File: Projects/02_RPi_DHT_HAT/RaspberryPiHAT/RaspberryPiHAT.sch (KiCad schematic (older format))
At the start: 9 parts, among them J1 Raspberry_Pi_2_3, SW1 SW_DPST, U1 DHT22

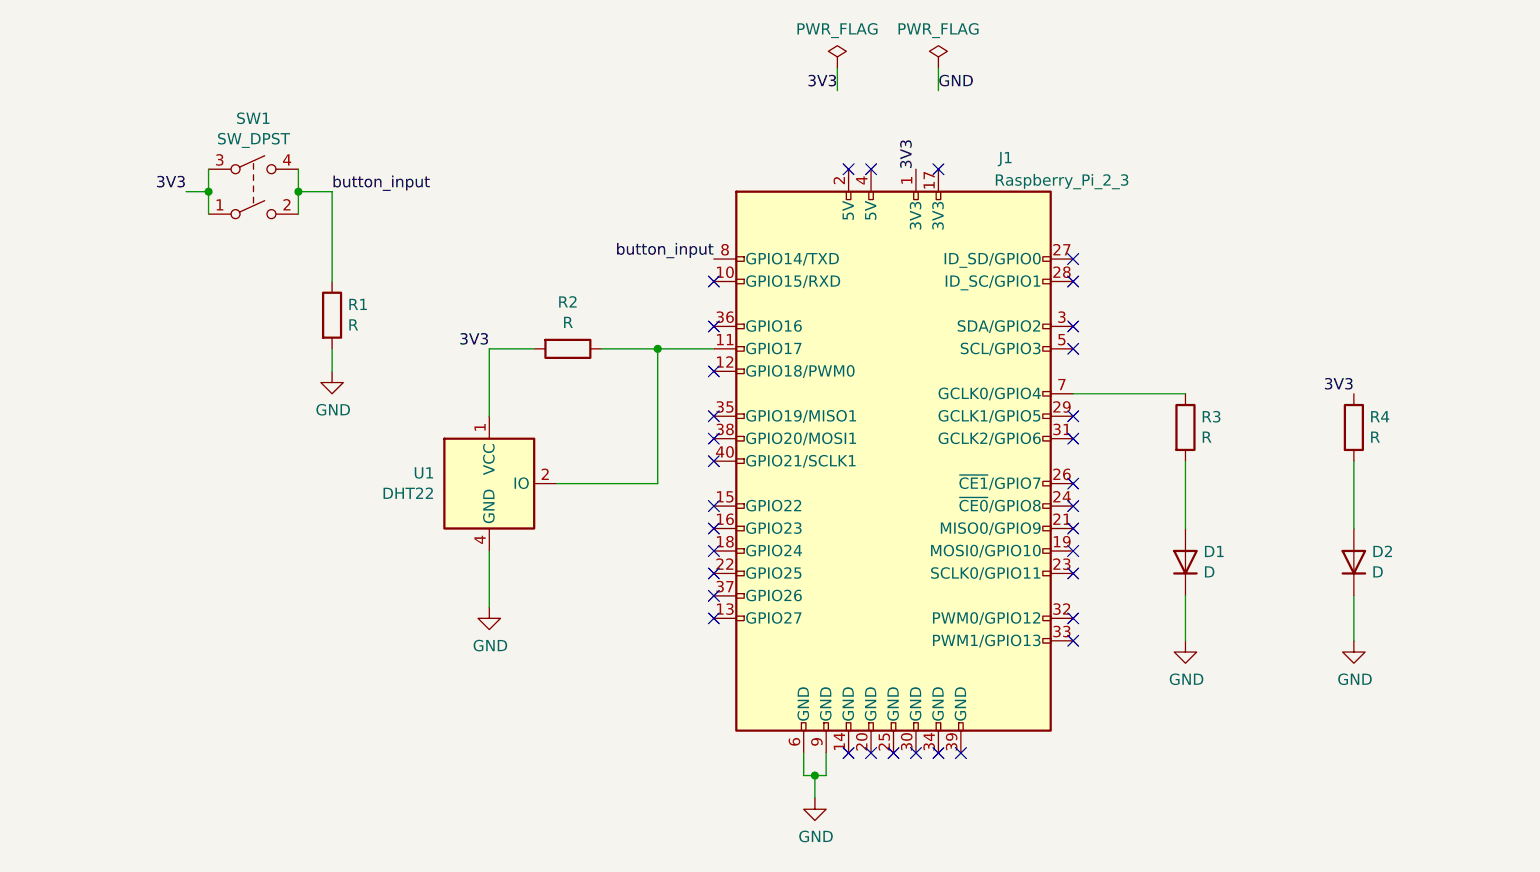
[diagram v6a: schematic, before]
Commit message: Project 2: Add comments on schematic
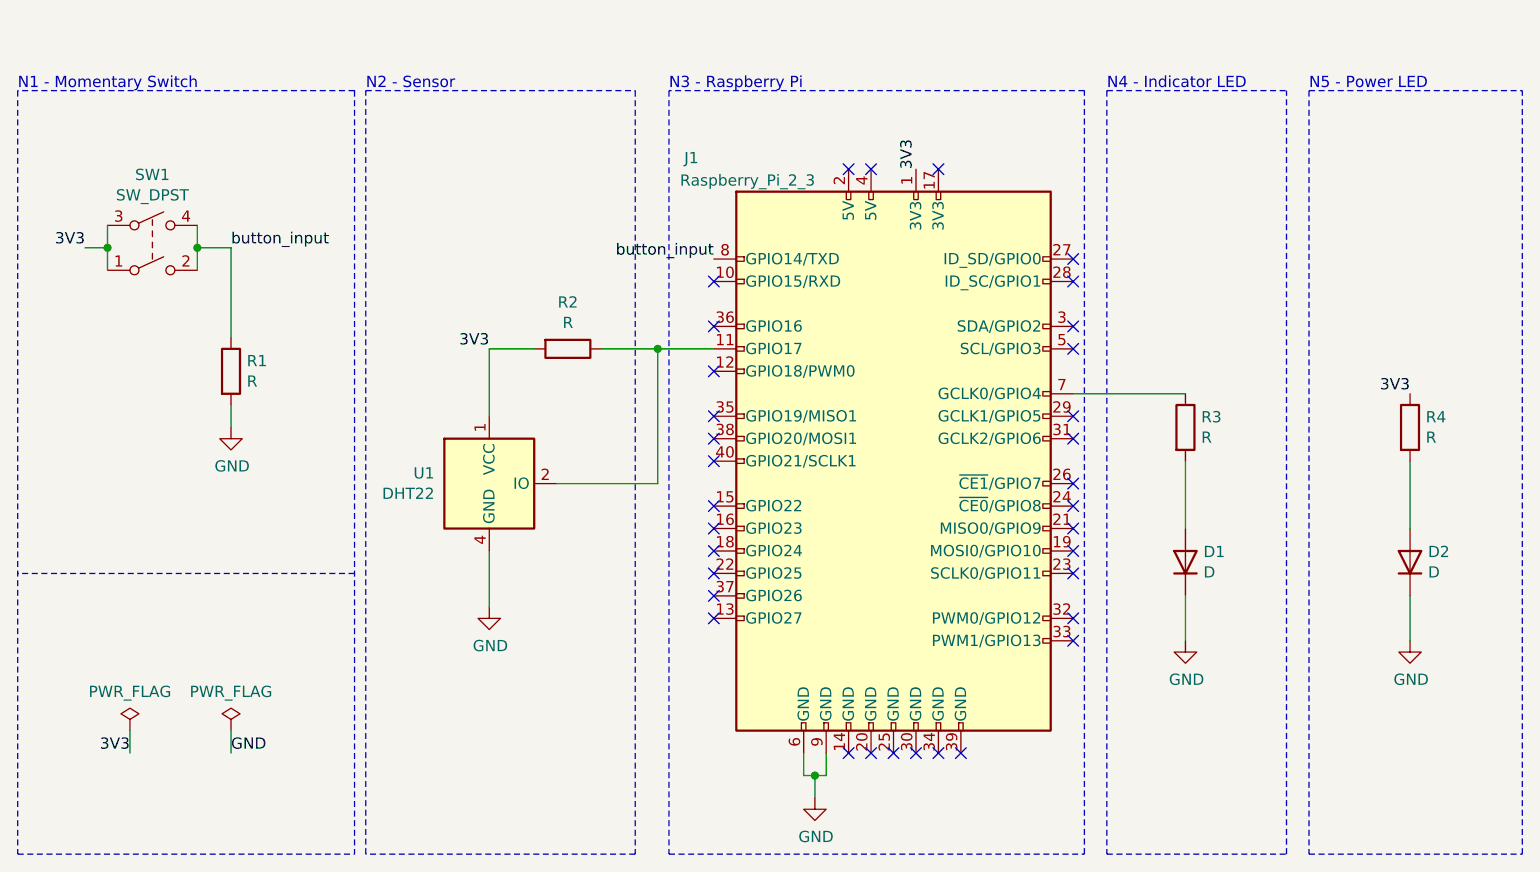
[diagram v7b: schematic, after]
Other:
- note added: "N1 - Momentary Switch"
- note added: "N2 - Sensor"
- note added: "N3 - Raspberry Pi"
- note added: "N4 - Indicator LED"
- note added: "N5 - Power LED"
- moved on the sheet: D2, R1, R4, SW1
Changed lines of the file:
@@
 U 1 1 61CF6995
 P 5550 3750
-F 0 "J1" H 6050 5100 50  0000 C CNN
-F 1 "Raspberry_Pi_2_3" H 6300 5000 50  0000 C CNN
+F 0 "J1" H 4650 5100 50  0000 C CNN
+F 1 "Raspberry_Pi_2_3" H 4900 5000 50  0000 C CNN
 F 2 "Connector_PinSocket_2.54mm:PinSocket_2x08_P2.54mm_Vertical" H 5550 3750 50  0001 C CNN
 F 3 "https://www.raspberrypi.org/documentation/hardware/raspberrypi/schematics/rpi_SCH_3bplus_1p0_reduced.pdf" H 5550 3750 50  0001 C CNN
@@
 Wire Wire Line
 	3750 4150 3750 4400
-Text Label 7600 3450 2    50   ~ 0
-3V3
-Wire Wire Line
-	7600 4550 7600 4350
+Wire Notes Line
+	3150 2100 1650 2100
+Text Label 2150 5050 2    50   ~ 0
+3V3
+Text Label 2600 5050 0    50   ~ 0
+GND
+Wire Wire Line
+	2600 4950 2600 5050
+Wire Wire Line
+	2150 4950 2150 5050
+$Comp
+L power:PWR_FLAG #FLG0102
+U 1 1 61D4FE8E
+P 2600 4950
+F 0 "#FLG0102" H 2600 5025 50  0001 C CNN
+F 1 "PWR_FLAG" H 2600 5123 50  0000 C CNN
+F 2 "" H 2600 4950 50  0001 C CNN
+F 3 "~" H 2600 4950 50  0001 C CNN
+	1    2600 4950
+	1    0    0    -1
+$EndComp
+$Comp
+L power:PWR_FLAG #FLG0101
+U 1 1 61D30DD8
+P 2150 4950
+F 0 "#FLG0101" H 2150 5025 50  0001 C CNN
+F 1 "PWR_FLAG" H 2150 5123 50  0000 C CNN
+F 2 "" H 2150 4950 50  0001 C CNN
+F 3 "~" H 2150 4950 50  0001 C CNN
+	1    2150 4950
+	1    0    0    -1
+$EndComp
+$Comp
+L Device:R R1
+U 1 1 61CFF65D
+P 2600 3350
+F 0 "R1" H 2670 3396 50  0000 L CNN
+F 1 "R" H 2670 3305 50  0000 L CNN
+F 2 "Resistor_SMD:R_0805_2012Metric" V 2530 3350 50  0001 C CNN
+F 3 "~" H 2600 3350 50  0001 C CNN
+	1    2600 3350
+	1    0    0    -1
+$EndComp
+$Comp
+L Switch:SW_DPST SW1
+U 1 1 61D01499
+P 2250 2800
+F 0 "SW1" H 2250 3125 50  0000 C CNN
+F 1 "SW_DPST" H 2250 3034 50  0000 C CNN
+F 2 "freetronics_footprints:SW_PUSHBUTTON_PTH" H 2250 2800 50  0001 C CNN
+F 3 "~" H 2250 2800 50  0001 C CNN
+	1    2250 2800
+	1    0    0    -1
+$EndComp
+Wire Wire Line
+	2450 2700 2450 2800
+Connection ~ 2450 2800
+Wire Wire Line
+	2450 2800 2450 2900
+Wire Wire Line
+	2450 2800 2600 2800
+Wire Wire Line
+	2600 3200 2600 2800
+Wire Wire Line
+	2050 2700 2050 2800
+$Comp
+L power:GND #PWR0102
+U 1 1 61D4400F
+P 2600 3600
+F 0 "#PWR0102" H 2600 3350 50  0001 C CNN
+F 1 "GND" H 2605 3427 50  0000 C CNN
+F 2 "" H 2600 3600 50  0001 C CNN
+F 3 "" H 2600 3600 50  0001 C CNN
+	1    2600 3600
+	1    0    0    -1
+$EndComp
+Wire Wire Line
+	2600 3500 2600 3600
+Text Label 2600 2800 0    50   ~ 0
+button_input
+Wire Wire Line
+	2050 2800 1950 2800
+Connection ~ 2050 2800
+Wire Wire Line
+	2050 2800 2050 2900
+Text Label 1950 2800 2    50   ~ 0
+3V3
+Wire Notes Line
+	3150 4250 1650 4250
+Wire Notes Line
+	3200 2100 4400 2100
+Wire Notes Line
+	4400 2100 4400 5500
+Wire Notes Line
+	4400 5500 3200 5500
+Wire Notes Line
+	3200 5500 3200 2100
+Wire Notes Line
+	4550 2100 4550 5500
+Wire Notes Line
+	4550 5500 6400 5500
+Wire Notes Line
+	6400 5500 6400 2100
+Wire Notes Line
+	6400 2100 4550 2100
+Wire Notes Line
+	6500 2100 6500 5500
+Text Notes 1650 2100 0    50   ~ 0
+N1 - Momentary Switch
+Text Notes 3200 2100 0    50   ~ 0
+N2 - Sensor
+Text Notes 4550 2100 0    50   ~ 0
+N3 - Raspberry Pi
+Wire Notes Line
+	7300 5500 7300 2100
+Wire Notes Line
+	6500 2100 7300 2100
+Wire Notes Line
+	6500 5500 7300 5500
+Text Notes 6500 2100 0    50   ~ 0
+N4 - Indicator LED
+Wire Notes Line
+	7400 2100 7400 5500
+Wire Notes Line
+	8350 5500 8350 2100
+Wire Notes Line
+	7400 2100 8350 2100
+Wire Notes Line
+	7400 5500 8350 5500
+Text Notes 7400 2100 0    50   ~ 0
+N5 - Power LED
+$Comp
+L Device:R R4
+U 1 1 61D00A50
+P 7850 3600
+F 0 "R4" H 7920 3646 50  0000 L CNN
+F 1 "R" H 7920 3555 50  0000 L CNN
+F 2 "Resistor_SMD:R_0805_2012Metric" V 7780 3600 50  0001 C CNN
+F 3 "~" H 7850 3600 50  0001 C CNN
+	1    7850 3600
+	1    0    0    -1
+$EndComp
+$Comp
+L Device:D D2
+U 1 1 61D00BDA
+P 7850 4200
+F 0 "D2" V 7896 4120 50  0000 R CNN
+F 1 "D" V 7805 4120 50  0000 R CNN
+F 2 "LED_SMD:LED_0805_2012Metric" H 7850 4200 50  0001 C CNN
+F 3 "~" H 7850 4200 50  0001 C CNN
+	1    7850 4200
+	0    -1   -1   0
+$EndComp
+Wire Wire Line
+	7850 4050 7850 3750
 $Comp
 L power:GND #PWR01
 U 1 1 61D00BE6
-P 7600 4550
-F 0 "#PWR01" H 7600 4300 50  0001 C CNN
-F 1 "GND" H 7605 4377 50  0000 C CNN
-F 2 "" H 7600 4550 50  0001 C CNN
-F 3 "" H 7600 4550 50  0001 C CNN
-	1    7600 4550
-	1    0    0    -1
-$EndComp
-Wire Wire Line
-	7600 4050 7600 3750
-$Comp
-L Device:D D2
-U 1 1 61D00BDA
-P 7600 4200
-F 0 "D2" V 7646 4120 50  0000 R CNN
-F 1 "D" V 7555 4120 50  0000 R CNN
-F 2 "LED_SMD:LED_0805_2012Metric" H 7600 4200 50  0001 C CNN
-F 3 "~" H 7600 4200 50  0001 C CNN
-	1    7600 4200
-	0    -1   -1   0
-$EndComp
-$Comp
-L Device:R R4
-U 1 1 61D00A50
-P 7600 3600
-F 0 "R4" H 7670 3646 50  0000 L CNN
-F 1 "R" H 7670 3555 50  0000 L CNN
-F 2 "Resistor_SMD:R_0805_2012Metric" V 7530 3600 50  0001 C CNN
-F 3 "~" H 7600 3600 50  0001 C CNN
-	1    7600 3600
-	1    0    0    -1
-$EndComp
-$Comp
-L power:PWR_FLAG #FLG0101
-U 1 1 61D30DD8
-P 5300 2000
-F 0 "#FLG0101" H 5300 2075 50  0001 C CNN
-F 1 "PWR_FLAG" H 5300 2173 50  0000 C CNN
-F 2 "" H 5300 2000 50  0001 C CNN
-F 3 "~" H 5300 2000 50  0001 C CNN
-	1    5300 2000
-	1    0    0    -1
-$EndComp
-$Comp
-L power:PWR_FLAG #FLG0102
-U 1 1 61D4FE8E
-P 5750 2000
-F 0 "#FLG0102" H 5750 2075 50  0001 C CNN
-F 1 "PWR_FLAG" H 5750 2173 50  0000 C CNN
-F 2 "" H 5750 2000 50  0001 C CNN
-F 3 "~" H 5750 2000 50  0001 C CNN
-	1    5750 2000
-	1    0    0    -1
-$EndComp
-Wire Wire Line
-	5300 2000 5300 2100
-Wire Wire Line
-	5750 2000 5750 2100
-Text Label 5750 2100 0    50   ~ 0
-GND
-Text Label 5300 2100 2    50   ~ 0
-3V3
-Text Label 2400 2550 2    50   ~ 0
-3V3
-Wire Wire Line
-	2500 2550 2500 2650
-Connection ~ 2500 2550
-Wire Wire Line
-	2500 2550 2400 2550
-Text Label 3050 2550 0    50   ~ 0
-button_input
-Wire Wire Line
-	3050 3250 3050 3350
-$Comp
-L power:GND #PWR0102
-U 1 1 61D4400F
-P 3050 3350
-F 0 "#PWR0102" H 3050 3100 50  0001 C CNN
-F 1 "GND" H 3055 3177 50  0000 C CNN
-F 2 "" H 3050 3350 50  0001 C CNN
-F 3 "" H 3050 3350 50  0001 C CNN
-	1    3050 3350
-	1    0    0    -1
-$EndComp
-Wire Wire Line
-	2500 2450 2500 2550
-Wire Wire Line
-	3050 2950 3050 2550
-Wire Wire Line
-	2900 2550 3050 2550
-Wire Wire Line
-	2900 2550 2900 2650
-Connection ~ 2900 2550
-Wire Wire Line
-	2900 2450 2900 2550
-$Comp
-L Switch:SW_DPST SW1
-U 1 1 61D01499
-P 2700 2550
-F 0 "SW1" H 2700 2875 50  0000 C CNN
-F 1 "SW_DPST" H 2700 2784 50  0000 C CNN
-F 2 "freetronics_footprints:SW_PUSHBUTTON_PTH" H 2700 2550 50  0001 C CNN
-F 3 "~" H 2700 2550 50  0001 C CNN
-	1    2700 2550
-	1    0    0    -1
-$EndComp
-$Comp
-L Device:R R1
-U 1 1 61CFF65D
-P 3050 3100
-F 0 "R1" H 3120 3146 50  0000 L CNN
-F 1 "R" H 3120 3055 50  0000 L CNN
-F 2 "Resistor_SMD:R_0805_2012Metric" V 2980 3100 50  0001 C CNN
-F 3 "~" H 3050 3100 50  0001 C CNN
-	1    3050 3100
-	1    0    0    -1
-$EndComp
+P 7850 4550
+F 0 "#PWR01" H 7850 4300 50  0001 C CNN
+F 1 "GND" H 7855 4377 50  0000 C CNN
+F 2 "" H 7850 4550 50  0001 C CNN
+F 3 "" H 7850 4550 50  0001 C CNN
+	1    7850 4550
+	1    0    0    -1
+$EndComp
+Wire Wire Line
+	7850 4550 7850 4350
+Text Label 7850 3450 2    50   ~ 0
+3V3
+Wire Notes Line
+	3150 2100 3150 5500
+Wire Notes Line
+	1650 2100 1650 5500
+Wire Notes Line
+	1650 5500 3150 5500
 $EndSCHEMATC

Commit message: Project 2: Edit footprint from socket to header for RPi in Eeschema
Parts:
- J1: footprint Connector_PinSocket_2.54mm:PinSocket_2x08_P2.54mm_Vertical -> Connector_PinHeader_2.54mm:PinHeader_2x08_P2.54mm_Vertical
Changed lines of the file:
@@
 F 0 "J1" H 4650 5100 50  0000 C CNN
 F 1 "Raspberry_Pi_2_3" H 4900 5000 50  0000 C CNN
-F 2 "Connector_PinSocket_2.54mm:PinSocket_2x08_P2.54mm_Vertical" H 5550 3750 50  0001 C CNN
+F 2 "Connector_PinHeader_2.54mm:PinHeader_2x08_P2.54mm_Vertical" H 5550 3750 50  0001 C CNN
 F 3 "https://www.raspberrypi.org/documentation/hardware/raspberrypi/schematics/rpi_SCH_3bplus_1p0_reduced.pdf" H 5550 3750 50  0001 C CNN
 	1    5550 3750
